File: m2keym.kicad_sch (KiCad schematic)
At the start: 14 parts, among them J8 Bus_M.2_1-2199230-6

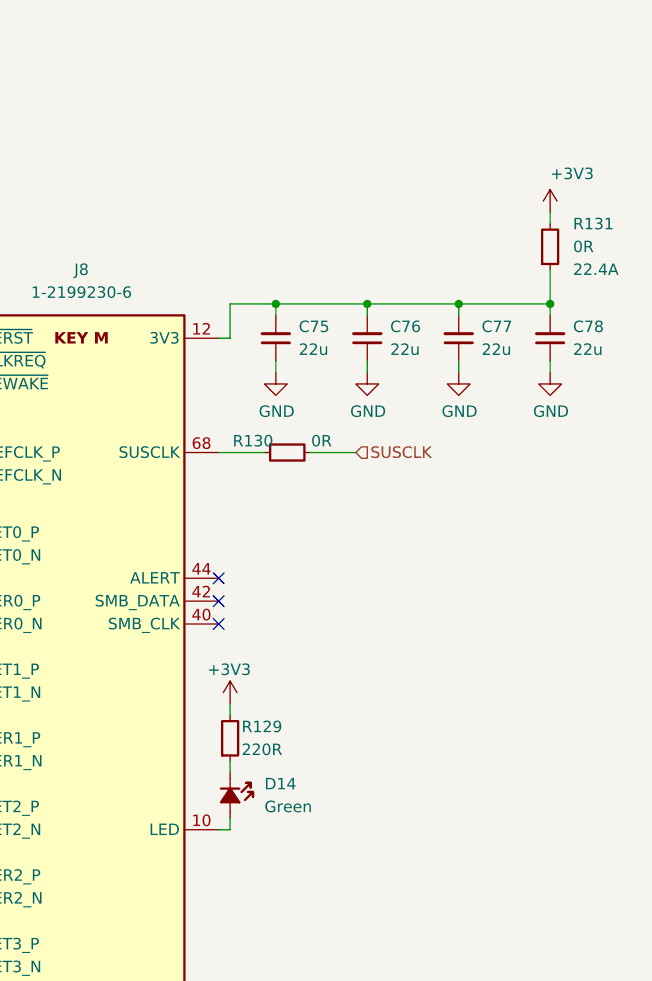
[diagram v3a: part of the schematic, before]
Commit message: [#65447] Fix rotated LEDs, overlapping text and symbols, add rules
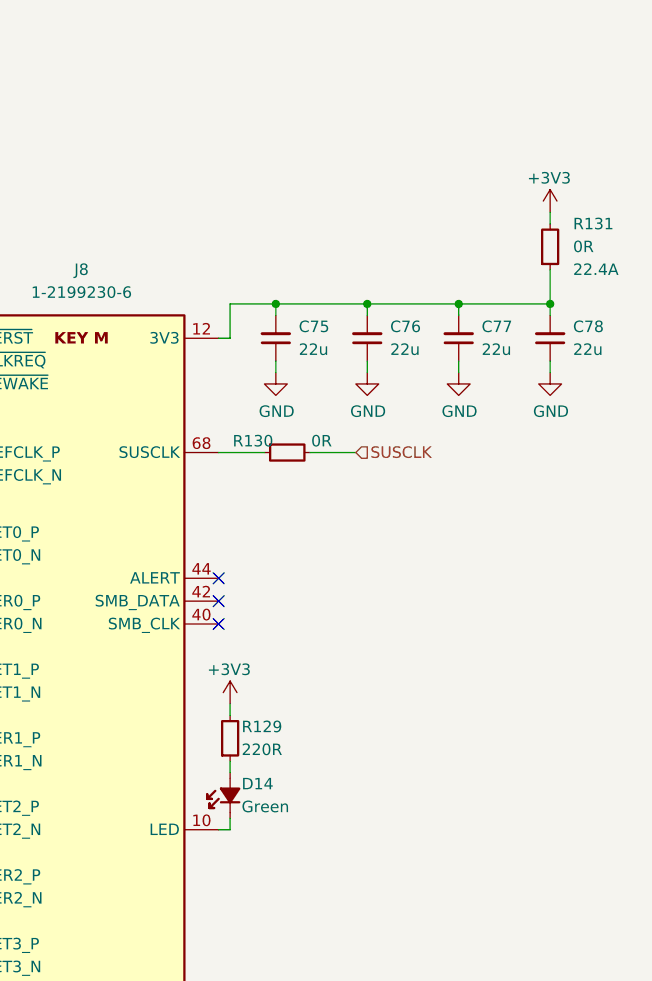
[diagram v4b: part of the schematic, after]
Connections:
- net at R129.1: now also D14.2 (A); no longer D14.1 (C)
- net at J8.10 (LED): now also D14.1 (C); no longer D14.2 (A)
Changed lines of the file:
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@@
   )
   (symbol (lib_id "antmicropower:+3V3") (at 267.97 74.93 0) (unit 1)
-    (in_bom yes) (on_board yes) (dnp no) (fields_autoplaced)
+    (in_bom yes) (on_board yes) (dnp no)
     (property "Reference" "#PWR0172" (at 267.97 78.74 0)
       (effects (font (size 1.27 1.27)) (justify left bottom) hide)
     )
-    (property "Value" "+3V3" (at 267.97 71.374 0)
-      (effects (font (size 1.27 1.27)) (justify left bottom))
+    (property "Value" "+3V3" (at 265.43 71.12 0)
+      (effects (font (size 1.27 1.27)) (justify left))
     )
     (property "Footprint" "" (at 267.97 74.93 0)
@@
     )
   )
-  (symbol (lib_id "antmicroLEDIndicationDiscrete:LED_G_0603_LTST-C190GKT") (at 232.41 137.16 270) (unit 1)
-    (in_bom yes) (on_board yes) (dnp no) (fields_autoplaced)
-    (property "Reference" "D14" (at 236.22 138.43 90)
-      (effects (font (size 1.27 1.27)) (justify left))
-    )
-    (property "Value" "LED_G_0603_LTST-C190GKT" (at 236.22 139.7 0)
-      (effects (font (size 1.27 1.27) (thickness 0.15)) (justify left bottom) hide)
-    )
-    (property "Footprint" "antmicro-footprints:LED_0603_1608Metric_G" (at 222.25 160.02 0)
-      (effects (font (size 1.27 1.27) (thickness 0.15)) (justify left bottom) hide)
-    )
-    (property "Datasheet" "https://media.digikey.com/pdf/Data%20Sheets/Lite-On%20PDFs/LTST-C190GKT.pdf" (at 219.71 160.02 0)
-      (effects (font (size 1.27 1.27) (thickness 0.15)) (justify left bottom) hide)
-    )
-    (property "MPN" "LTST-C190GKT" (at 235.585 142.875 90)
-      (effects (font (size 1.27 1.27) (thickness 0.15)) (justify left bottom) hide)
-    )
-    (property "Manufacturer" "Lite-On" (at 214.63 160.02 0)
-      (effects (font (size 1.27 1.27) (thickness 0.15)) (justify left bottom) hide)
-    )
-    (property "Author" "Antmicro" (at 212.09 160.02 0)
-      (effects (font (size 1.27 1.27) (thickness 0.15)) (justify left bottom) hide)
-    )
-    (property "License" "Apache-2.0" (at 209.55 160.02 0)
-      (effects (font (size 1.27 1.27) (thickness 0.15)) (justify left bottom) hide)
-    )
-    (property "Public" "False" (at 214.63 157.48 0)
-      (effects (font (size 1.27 1.27)) (justify left bottom) hide)
-    )
-    (property "Color" "Green" (at 236.22 140.97 90)
-      (effects (font (size 1.27 1.27)) (justify left))
-    )
-    (pin "1")
+  (symbol (lib_id "antmicroLEDIndicationDiscrete:LED_G_0603_LTST-C190GKT") (at 232.41 142.24 90) (unit 1)
+    (in_bom yes) (on_board yes) (dnp no)
+    (property "Reference" "D14" (at 233.68 138.43 90)
+      (effects (font (size 1.27 1.27)) (justify right))
+    )
+    (property "Value" "LED_G_0603_LTST-C190GKT" (at 228.6 139.7 0)
+      (effects (font (size 1.27 1.27) (thickness 0.15)) (justify left bottom) hide)
+    )
+    (property "Footprint" "antmicro-footprints:LED_0603_1608Metric_G" (at 242.57 119.38 0)
+      (effects (font (size 1.27 1.27) (thickness 0.15)) (justify left bottom) hide)
+    )
+    (property "Datasheet" "https://media.digikey.com/pdf/Data%20Sheets/Lite-On%20PDFs/LTST-C190GKT.pdf" (at 245.11 119.38 0)
+      (effects (font (size 1.27 1.27) (thickness 0.15)) (justify left bottom) hide)
+    )
+    (property "MPN" "LTST-C190GKT" (at 229.235 136.525 90)
+      (effects (font (size 1.27 1.27) (thickness 0.15)) (justify left bottom) hide)
+    )
+    (property "Manufacturer" "Lite-On" (at 250.19 119.38 0)
+      (effects (font (size 1.27 1.27) (thickness 0.15)) (justify left bottom) hide)
+    )
+    (property "Author" "Antmicro" (at 252.73 119.38 0)
+      (effects (font (size 1.27 1.27) (thickness 0.15)) (justify left bottom) hide)
+    )
+    (property "License" "Apache-2.0" (at 255.27 119.38 0)
+      (effects (font (size 1.27 1.27) (thickness 0.15)) (justify left bottom) hide)
+    )
+    (property "Public" "False" (at 250.19 121.92 0)
+      (effects (font (size 1.27 1.27)) (justify left bottom) hide)
+    )
+    (property "Color" "Green" (at 233.68 140.97 90)
+      (effects (font (size 1.27 1.27)) (justify right))
+    )
+    (pin "1")

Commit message: [#65840] Roughly route PCIe, GbE
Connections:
- net PCIe_{x4}.RX0+: now also J8.41 (PER0_N); no longer J8.43 (PER0_P)
- net PCIe_{x4}.RX0-: now also J8.43 (PER0_P); no longer J8.41 (PER0_N)
- net PCIe_{x4}.RX1+: now also J8.29 (PER1_N); no longer J8.31 (PER1_P)
- net PCIe_{x4}.RX1-: now also J8.31 (PER1_P); no longer J8.29 (PER1_N)
- net PCIe_{x4}.RX2+: now also J8.17 (PER2_N); no longer J8.19 (PER2_P)
- net PCIe_{x4}.RX2-: now also J8.19 (PER2_P); no longer J8.17 (PER2_N)
- net PCIe_{x4}.RX3+: now also J8.5 (PER3_N); no longer J8.7 (PER3_P)
- net PCIe_{x4}.RX3-: now also J8.7 (PER3_P); no longer J8.5 (PER3_N)
- net PCIe_{x4}.TX0+: now also J8.47 (PET0_N); no longer J8.49 (PET0_P)
- net PCIe_{x4}.TX0-: now also J8.49 (PET0_P); no longer J8.47 (PET0_N)
- net PCIe_{x4}.TX1+: now also J8.35 (PET1_N); no longer J8.37 (PET1_P)
- net PCIe_{x4}.TX1-: now also J8.37 (PET1_P); no longer J8.35 (PET1_N)
- net PCIe_{x4}.TX2+: now also J8.23 (PET2_N); no longer J8.25 (PET2_P)
- net PCIe_{x4}.TX2-: now also J8.25 (PET2_P); no longer J8.23 (PET2_N)
- net PCIe_{x4}.TX3+: now also J8.11 (PET3_N); no longer J8.13 (PET3_P)
- net PCIe_{x4}.TX3-: now also J8.13 (PET3_P); no longer J8.11 (PET3_N)
- net M2_3V3: now reaches C75.2, C76.2, C77.2, C78.2, J8.12 (3V3), J8.14 (3V3), J8.16 (3V3), J8.18 (3V3), J8.2 (3V3), J8.4 (3V3), J8.70 (3V3), J8.72 (3V3), J8.74 (3V3), R131.1
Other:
- note added: "Swapped polarity of TX and RX lines for easier PCB layout"
